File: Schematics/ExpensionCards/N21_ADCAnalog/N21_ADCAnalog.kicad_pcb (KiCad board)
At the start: 2 copper layers, 97.5 x 63.3 mm, 67 parts

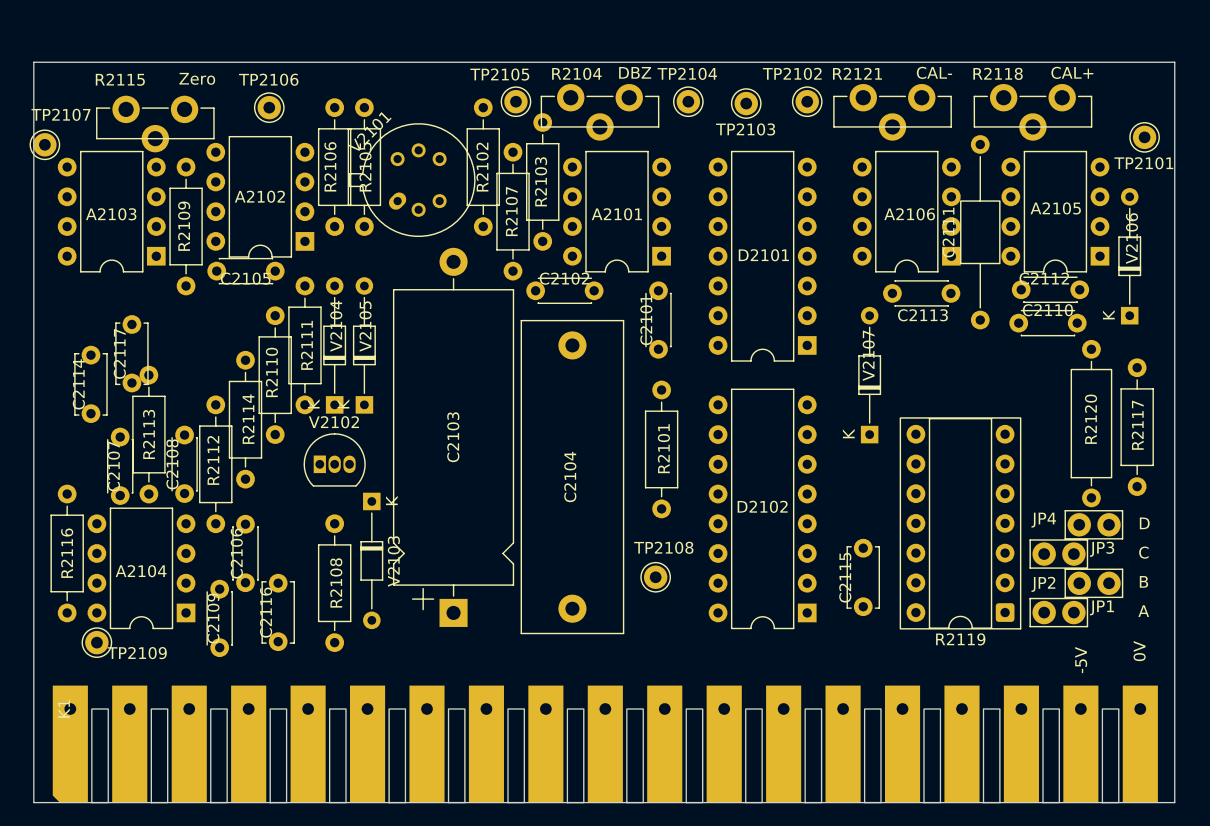
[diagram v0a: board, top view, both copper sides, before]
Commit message: Reworked N20/N21
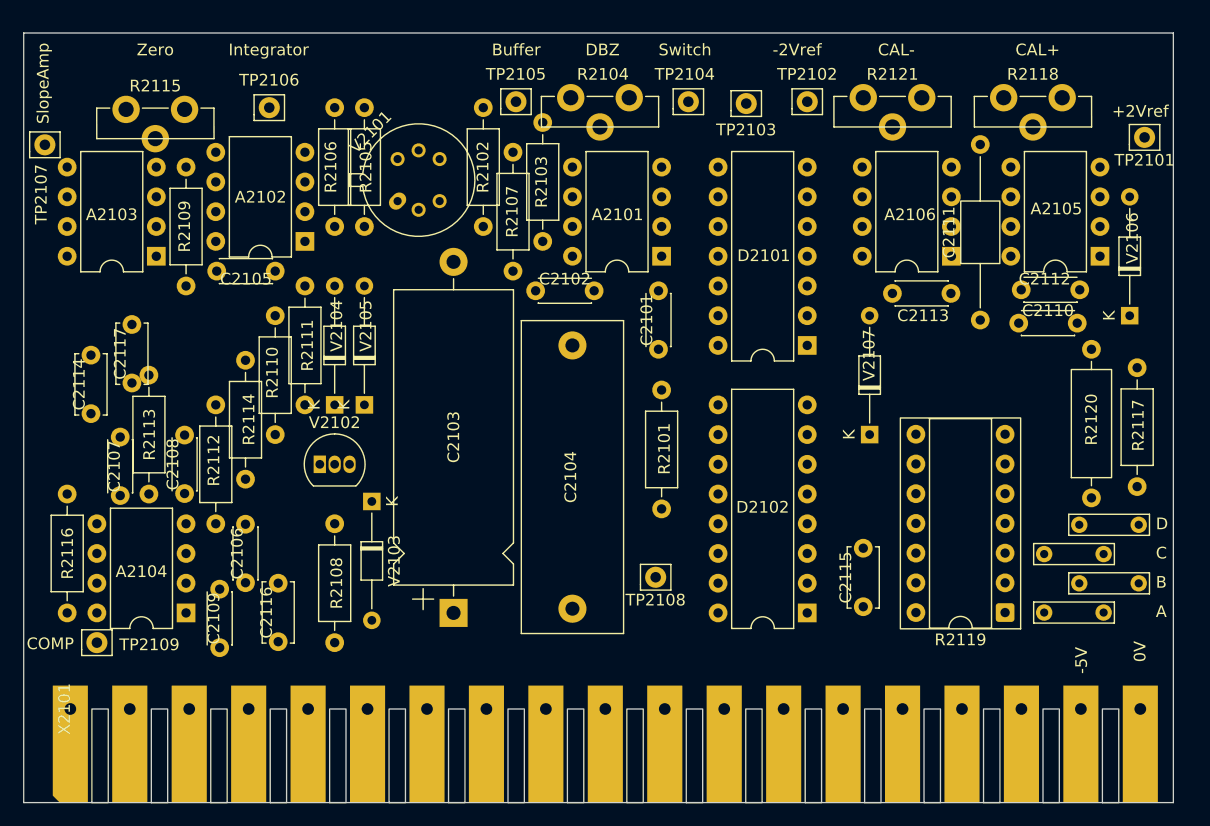
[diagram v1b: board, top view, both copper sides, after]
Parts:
- JP2101: renamed from JP1; value Jumper_2_Small_Bridged -> A; footprint TestPoint:TestPoint_Bridge_Pitch2.54mm_Drill1.0mm -> TestPoint:TestPoint_Bridge_Pitch5.08mm_Drill0.7mm
- JP2102: renamed from JP2; value Jumper_2_Small_Bridged -> B; footprint TestPoint:TestPoint_Bridge_Pitch2.54mm_Drill1.0mm -> TestPoint:TestPoint_Bridge_Pitch5.08mm_Drill0.7mm
- JP2103: renamed from JP3; value Jumper_2_Small_Bridged -> C; footprint TestPoint:TestPoint_Bridge_Pitch2.54mm_Drill1.0mm -> TestPoint:TestPoint_Bridge_Pitch5.08mm_Drill0.7mm
- JP2104: renamed from JP4; value Jumper_2_Small_Bridged -> D; footprint TestPoint:TestPoint_Bridge_Pitch2.54mm_Drill1.0mm -> TestPoint:TestPoint_Bridge_Pitch5.08mm_Drill0.7mm
- R2104, R2115, R2118, R2121: footprint PM2528:Potentiometer horizontal ceramic -> PM2528:Trimmer vertical
- R2105, R2106: value 82k5 -> 21M1
- R2111: value 5k9 -> 5k90
- TP2101, TP2102, TP2103, TP2104, TP2105, TP2106, TP2107, TP2108, TP2109: footprint Connector_Pin:Pin_D1.0mm_L10.0mm -> Connector_Pin:Pin_D0.9mm_L10.0mm_W2.4mm_FlatFork
- renumbered K1 to X2101
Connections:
- A2102 pad 6: Net-(A2102-BAL) -> Net-(A2102-Pad6)
- C2103 pad 1: Net-(A2102-BAL) -> Net-(A2102-Pad6)
- R2109 pad 1: Net-(A2102-BAL) -> Net-(A2102-Pad6)
- TP2106 pad 1: Net-(A2102-BAL) -> Net-(A2102-Pad6)
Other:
- board size 97.5 x 63.3 mm -> 98.2 x 65.8 mm
- board text added: "+2Vref"
- board text added: "-2Vref"
- board text added: "Buffer"
- board text added: "COMP"
- board text added: "Integrator"
- board text added: "SlopeAmp"
- board text added: "Switch"
